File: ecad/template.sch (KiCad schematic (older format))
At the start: 3 parts, among them P1 CF_EXP_LEFT, P2 CF_EXP_RIGHT

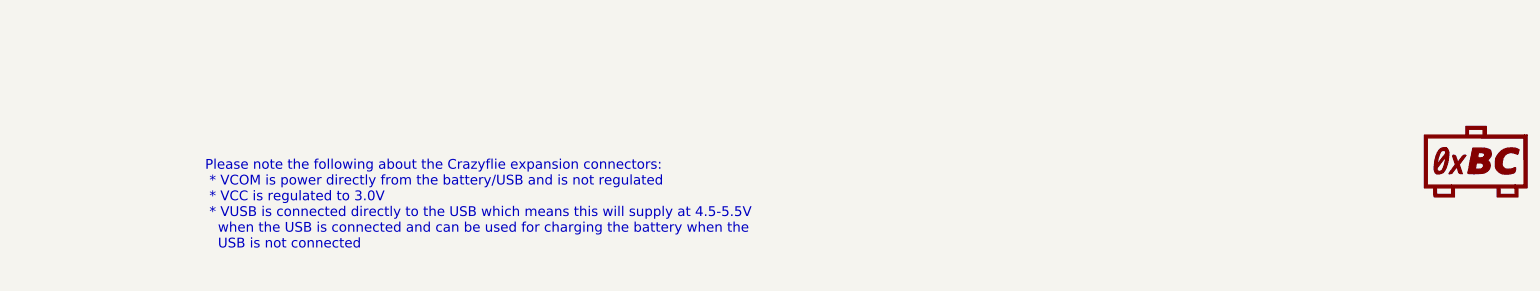
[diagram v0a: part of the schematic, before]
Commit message: Updated to new CF2 deck footprint which works better for SMT production.
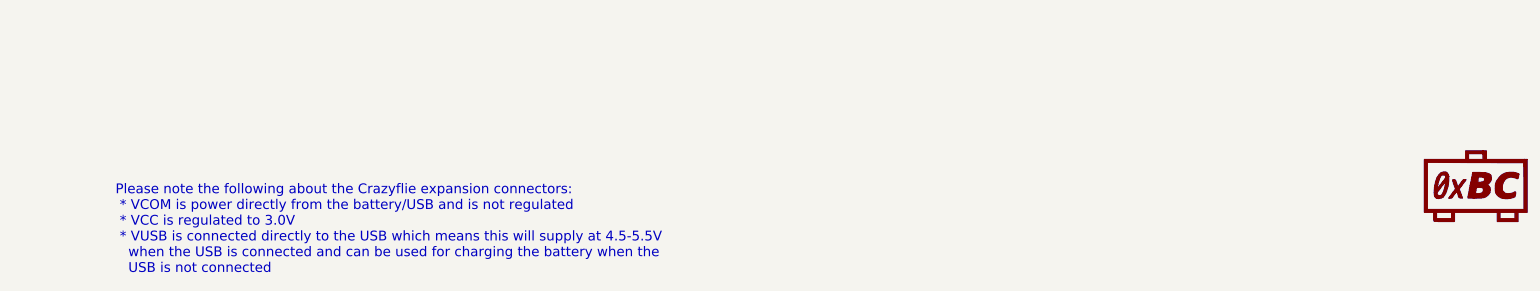
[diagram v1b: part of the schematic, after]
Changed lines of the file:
@@
 LIBS:contrib
 LIBS:valves
+LIBS:wireless
+LIBS:regulators
+LIBS:my_power
+LIBS:power_ic
+LIBS:usb_ic
+LIBS:sensors
+LIBS:imu_ic
+LIBS:mcu-st
+LIBS:connectors
+LIBS:bc-memory
+LIBS:xtal
+LIBS:bitcraze
 LIBS:template-cache
-EELAYER 27 0
+EELAYER 24 0
 EELAYER END
 $Descr A4 11693 8268
@@
 Sheet 1 1
 Title "Crazyflie 2.0 expansion boad template"
-Date "30 jan 2015"
+Date "20 okt 2014"
 Rev "A"
 Comp "Bitcraze AB"
@@
 	1    0    0    -1
 $EndComp
-Text Notes 2950 7200 0    60   ~ 0
+Text Notes 2400 7350 0    60   ~ 0
 Please note the following about the Crazyflie expansion connectors:\n * VCOM is power directly from the battery/USB and is not regulated\n * VCC is regulated to 3.0V\n * VUSB is connected directly to the USB which means this will supply at 4.5-5.5V\n   when the USB is connected and can be used for charging the battery when the\n   USB is not connected
 $Comp
 L bitcraze_200 B1
 U 1 1 543BE6EC
-P 10750 6650
-F 0 "B1" H 10750 6347 60  0001 C CNN
-F 1 "bitcraze_200" H 10750 6953 60  0001 C CNN
-F 2 "" H 10750 6650 60  0000 C CNN
-F 3 "" H 10750 6650 60  0000 C CNN
-	1    10750 6650
+P 10750 6800
+F 0 "B1" H 10750 6497 60  0001 C CNN
+F 1 "bitcraze_200" H 10750 7103 60  0001 C CNN
+F 2 "" H 10750 6800 60  0000 C CNN
+F 3 "" H 10750 6800 60  0000 C CNN
+	1    10750 6800
 	1    0    0    -1
 $EndComp

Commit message: Expansion connector lib added and project updated to use this.
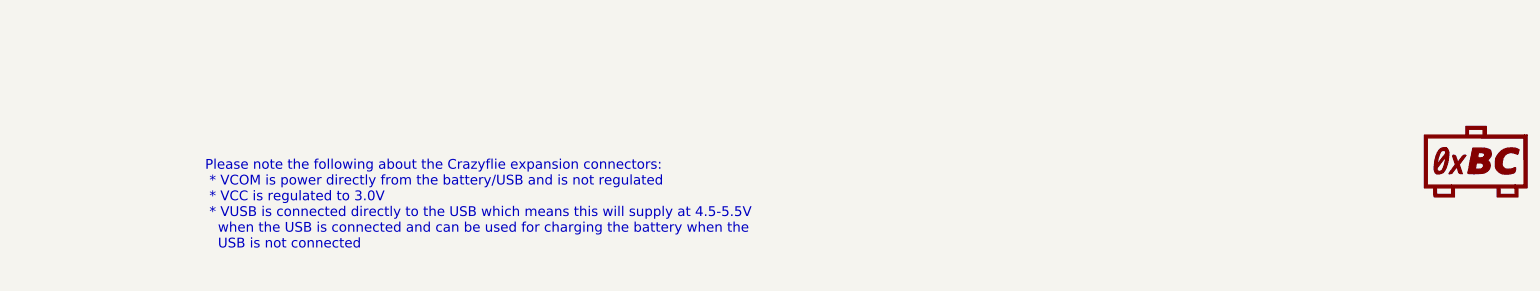
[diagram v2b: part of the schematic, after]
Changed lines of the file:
@@
 LIBS:contrib
 LIBS:valves
-LIBS:wireless
-LIBS:regulators
-LIBS:my_power
-LIBS:power_ic
-LIBS:usb_ic
-LIBS:sensors
-LIBS:imu_ic
-LIBS:mcu-st
-LIBS:connectors
-LIBS:bc-memory
-LIBS:xtal
-LIBS:bitcraze
 LIBS:template-cache
-EELAYER 24 0
+EELAYER 27 0
 EELAYER END
 $Descr A4 11693 8268
@@
 Sheet 1 1
 Title "Crazyflie 2.0 expansion boad template"
-Date "20 okt 2014"
+Date "30 jan 2015"
 Rev "A"
 Comp "Bitcraze AB"
@@
 	1    0    0    -1
 $EndComp
-Text Notes 2400 7350 0    60   ~ 0
+Text Notes 2950 7200 0    60   ~ 0
 Please note the following about the Crazyflie expansion connectors:\n * VCOM is power directly from the battery/USB and is not regulated\n * VCC is regulated to 3.0V\n * VUSB is connected directly to the USB which means this will supply at 4.5-5.5V\n   when the USB is connected and can be used for charging the battery when the\n   USB is not connected
 $Comp
 L bitcraze_200 B1
 U 1 1 543BE6EC
-P 10750 6800
-F 0 "B1" H 10750 6497 60  0001 C CNN
-F 1 "bitcraze_200" H 10750 7103 60  0001 C CNN
-F 2 "" H 10750 6800 60  0000 C CNN
-F 3 "" H 10750 6800 60  0000 C CNN
-	1    10750 6800
+P 10750 6650
+F 0 "B1" H 10750 6347 60  0001 C CNN
+F 1 "bitcraze_200" H 10750 6953 60  0001 C CNN
+F 2 "" H 10750 6650 60  0000 C CNN
+F 3 "" H 10750 6650 60  0000 C CNN
+	1    10750 6650
 	1    0    0    -1
 $EndComp
